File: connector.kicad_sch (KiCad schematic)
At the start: 83 parts, among them J1 USB_C_Receptacle_USB2.0_16P, J10 POWER2, J11 TELEM1, J12 TELEM2, J13 GPS, J14 SERIAL4, J15 SERIAL5, J16 I2C, J17 CAN, J18 BUZZER, J19 SWD, J2 Micro_SD_Card_Det1, J20 ADC, J21 SPI, J22 SAFETY, J23 CAN2, J24 SBUS, J3 S_TOP_SIG, J4 S_TOP_PWR, J5 S_TOP_GND, J6 S_SIDE_SIG, J7 S_SIDE_PWR, J8 S_SIDE_GND, J9 POWER1, Q1 AO3400A, U12 USBLC6-2SC6

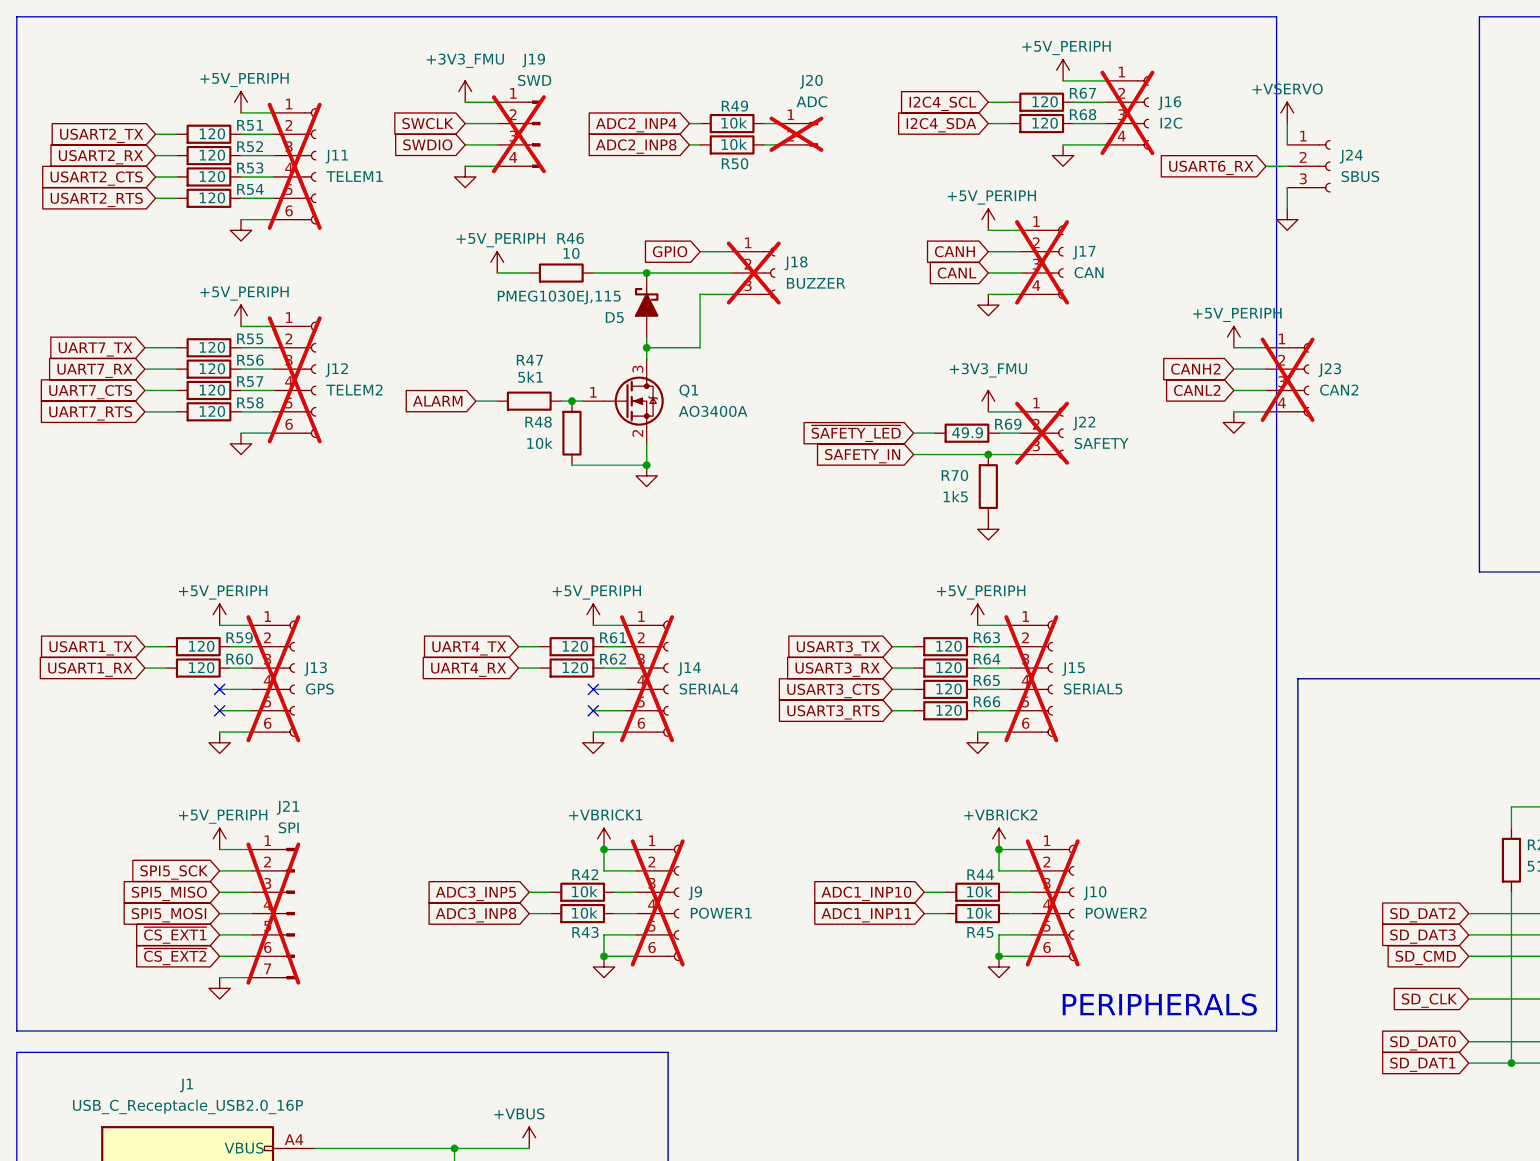
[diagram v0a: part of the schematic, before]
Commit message: Menyesuaikan Decoupling Cap, PullUp Resistor pada FM25CL64B, menambahkan RST Debugger.
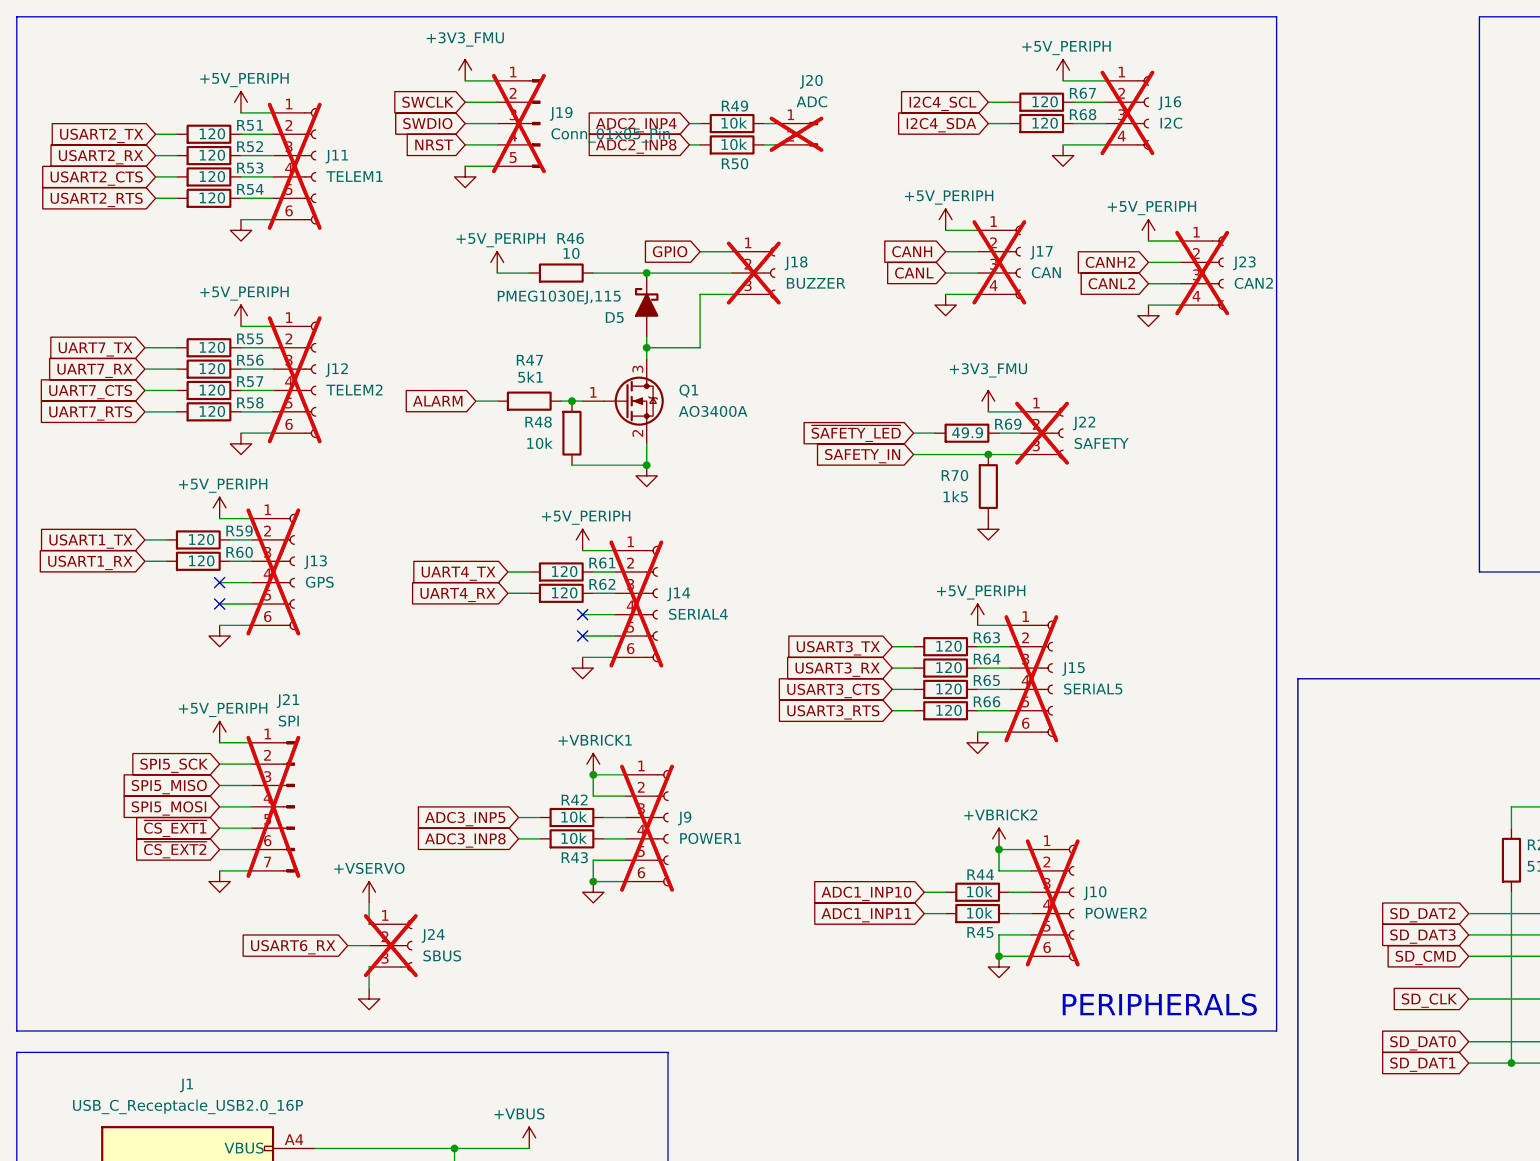
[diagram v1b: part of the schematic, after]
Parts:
- J19: value SWD -> Conn_01x05_Pin; symbol Connector:Conn_01x04_Pin -> Connector:Conn_01x05_Pin
- J24: now not fitted
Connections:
- net GND: now also J19.5 (Pin_5); no longer J19.4 (Pin_4)
- new net NRST: J19.4 (Pin_4)
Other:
- moved on the sheet: J13, J14, J17, J21, J23, J9, R42, R43, R59, R60, R61, R62

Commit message: Schematic Changes on MPN and Footprint
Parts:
- J19: footprint Connector_PinHeader_2.54mm:PinHeader_1x04_P2.54mm_Vertical -> Connector_PinHeader_2.54mm:PinHeader_1x05_P2.54mm_Vertical
- U12: MPN USBLC6-4SC6 -> USBLC6-2SC6
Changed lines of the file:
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@@
 			)
 		)
-		(property "MPN" "USBLC6-4SC6"
+		(property "MPN" "USBLC6-2SC6"
 			(at 66.04 163.83 0)
 			(hide yes)
@@
 		(in_pos_files yes)
 		(dnp yes)
-		(fields_autoplaced yes)
 		(property "Reference" "J19"
-			(at 77.47 25.3999 0)
-			(show_name no)
-			(do_not_autoplace no)
-			(effects
-				(font
-					(size 1.27 1.27)
-				)
-				(justify right)
+			(at 76.2 19.05 0)
+			(show_name no)
+			(do_not_autoplace no)
+			(effects
+				(font
+					(size 1.27 1.27)
+				)
 			)
 		)
 		(property "Value" "Conn_01x05_Pin"
-			(at 77.47 27.9399 0)
-			(show_name no)
-			(do_not_autoplace no)
-			(effects
-				(font
-					(size 1.27 1.27)
-				)
-				(justify right)
-			)
-		)
-		(property "Footprint" "Connector_PinHeader_2.54mm:PinHeader_1x04_P2.54mm_Vertical"
+			(at 76.2 34.29 0)
+			(show_name no)
+			(do_not_autoplace no)
+			(effects
+				(font
+					(size 1.27 1.27)
+				)
+			)
+		)
+		(property "Footprint" "Connector_PinHeader_2.54mm:PinHeader_1x05_P2.54mm_Vertical"
 			(at 76.2 26.67 0)
 			(hide yes)
@@
 			(at 76.2 26.67 0)
 			(hide yes)
-			(show_name no)
-			(do_not_autoplace no)
-			(effects
-				(font
-					(size 1.27 1.27)
-				)
-			)
-		)
-		(property "MPN" ""
-			(at 76.2 26.67 0)
-			(hide yes)

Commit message: Membuat library dan memperbaiki footprint pada schematic
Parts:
- J21: footprint Svayam:TestPoint_7Pads_2.0x2.0mm -> Connector_JST:JST_GH_BM07B-GHS-TBT_1x07-1MP_P1.25mm_Vertical
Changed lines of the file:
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@@
 			)
 		)
-		(property "Footprint" "Svayam:TestPoint_7Pads_2.0x2.0mm"
+		(property "Footprint" "Connector_JST:JST_GH_BM07B-GHS-TBT_1x07-1MP_P1.25mm_Vertical"
 			(at 46.99 107.95 0)
 			(hide yes)

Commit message: Mulai layout
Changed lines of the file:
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@@
 	)
 	(junction
-		(at 82.55 104.14)
-		(diameter 0)
-		(color 0 0 0 0)
-	)
-	(junction
 		(at 264.16 34.29)
 		(diameter 0)
@@
 	)
 	(junction
+		(at 82.55 104.14)
+		(diameter 0)
+		(color 0 0 0 0)
+	)
+	(junction
 		(at 264.16 36.83)
 		(diameter 0)
@@
 	)
 	(junction
-		(at 130.81 113.03)
-		(diameter 0)
-		(color 0 0 0 0)
-	)
-	(junction
 		(at 264.16 49.53)
 		(diameter 0)
@@
 	)
 	(junction
+		(at 130.81 113.03)
+		(diameter 0)
+		(color 0 0 0 0)
+	)
+	(junction
 		(at 246.38 64.77)
 		(diameter 0)
@@
 	(wire
 		(pts
+			(xy 118.11 111.76) (xy 118.11 113.03)
+		)
+		(stroke
+			(width 0)
+			(type default)
+		)
+	)
+	(wire
+		(pts
 			(xy 215.9 59.69) (xy 219.71 59.69)
 		)
@@
 	(wire
 		(pts
+			(xy 67.31 104.14) (xy 82.55 104.14)
+		)
+		(stroke
+			(width 0)
+			(type default)
+		)
+	)
+	(wire
+		(pts
 			(xy 81.28 77.47) (xy 85.09 77.47)
 		)
@@
 	(wire
 		(pts
+			(xy 118.11 113.03) (xy 130.81 113.03)
+		)
+		(stroke
+			(width 0)
+			(type default)
+		)
+	)
+	(wire
+		(pts
 			(xy 262.89 31.75) (xy 264.16 31.75)
 		)
@@
 	)
 	(symbol
+		(lib_id "power:+3V3")
+		(at 118.11 111.76 0)
+		(unit 1)
+		(body_style 1)
+		(exclude_from_sim no)
+		(in_bom yes)
+		(on_board yes)
+		(in_pos_files yes)
+		(dnp no)
+		(property "Reference" "#PWR082"
+			(at 118.11 115.57 0)
+			(hide yes)
+			(show_name no)
+			(do_not_autoplace no)
+			(effects
+				(font
+					(size 1.27 1.27)
+				)
+			)
+		)
+		(property "Value" "+VBRICK2"
+			(at 113.792 107.696 0)
+			(show_name no)
+			(do_not_autoplace no)
+			(effects
+				(font
+					(size 1.27 1.27)
+				)
+				(justify left)
+			)
+		)
+		(property "Footprint" ""
+			(at 118.11 111.76 0)
+			(hide yes)
+			(show_name no)
+			(do_not_autoplace no)
+			(effects
+				(font
+					(size 1.27 1.27)
+				)
+			)
+		)
+		(property "Datasheet" ""
+			(at 118.11 111.76 0)
+			(hide yes)
+			(show_name no)
+			(do_not_autoplace no)
+			(effects
+				(font
+					(size 1.27 1.27)
+				)
+			)
+		)
+		(property "Description" "Power symbol creates a global label with name \"+3V3\""
+			(at 118.11 111.76 0)
+			(hide yes)
+			(show_name no)
+			(do_not_autoplace no)
+			(effects
+				(font
+					(size 1.27 1.27)
+				)
+			)
+		)
+		(pin "1"
+		)
+		(instances
+			(project "SvayamV3_IIK"
+				(path "/2845b085-eb04-41a1-8594-b2a880ca4ab0/62301ec1-b8c7-4fa7-aee1-8dbd1d010312"
+					(reference "#PWR082")
+					(unit 1)
+				)
+			)
+		)
+	)
+	(symbol
 		(lib_id "Device:R")
 		(at 124.46 93.98 270)
@@
 	)
 	(symbol
-		(lib_id "power:+3V3")
-		(at 130.81 113.03 0)
-		(unit 1)
-		(body_style 1)
-		(exclude_from_sim no)
-		(in_bom yes)
-		(on_board yes)
-		(in_pos_files yes)
-		(dnp no)
-		(property "Reference" "#PWR082"
-			(at 130.81 116.84 0)
-			(hide yes)
-			(show_name no)
-			(do_not_autoplace no)
-			(effects
-				(font
-					(size 1.27 1.27)
-				)
-			)
-		)
-		(property "Value" "+VBRICK2"
-			(at 126.492 108.966 0)
-			(show_name no)
-			(do_not_autoplace no)
-			(effects
-				(font
-					(size 1.27 1.27)
-				)
-				(justify left)
-			)
-		)
-		(property "Footprint" ""
-			(at 130.81 113.03 0)
-			(hide yes)
-			(show_name no)
-			(do_not_autoplace no)
-			(effects
-				(font
-					(size 1.27 1.27)
-				)
-			)
-		)
-		(property "Datasheet" ""
-			(at 130.81 113.03 0)
-			(hide yes)
-			(show_name no)
-			(do_not_autoplace no)
-			(effects
-				(font
-					(size 1.27 1.27)
-				)
-			)
-		)
-		(property "Description" "Power symbol creates a global label with name \"+3V3\""
-			(at 130.81 113.03 0)
-			(hide yes)
-			(show_name no)
-			(do_not_autoplace no)
-			(effects
-				(font
-					(size 1.27 1.27)
-				)
-			)
-		)
-		(pin "1"
-		)
-		(instances
-			(project "SvayamV3_IIK"
-				(path "/2845b085-eb04-41a1-8594-b2a880ca4ab0/62301ec1-b8c7-4fa7-aee1-8dbd1d010312"
-					(reference "#PWR082")
-					(unit 1)
-				)
-			)
-		)
-	)
-	(symbol
 		(lib_id "power:GND")
 		(at 38.1 115.57 0)
@@
 	(symbol
 		(lib_id "power:+3V3")
-		(at 82.55 104.14 0)
+		(at 67.31 104.14 0)
 		(unit 1)
 		(body_style 1)
@@
 		(dnp no)
 		(property "Reference" "#PWR081"
-			(at 82.55 107.95 0)
+			(at 67.31 107.95 0)
 			(hide yes)
 			(show_name no)
@@
 		)
 		(property "Value" "+VBRICK1"
-			(at 78.232 100.076 0)
+			(at 62.992 100.076 0)
 			(show_name no)
 			(do_not_autoplace no)
@@
 		)
 		(property "Footprint" ""
-			(at 82.55 104.14 0)
+			(at 67.31 104.14 0)
 			(hide yes)
 			(show_name no)
@@
 		)
 		(property "Datasheet" ""
-			(at 82.55 104.14 0)
+			(at 67.31 104.14 0)
 			(hide yes)
 			(show_name no)
@@
 		)
 		(property "Description" "Power symbol creates a global label with name \"+3V3\""
-			(at 82.55 104.14 0)
+			(at 67.31 104.14 0)
 			(hide yes)
 			(show_name no)
